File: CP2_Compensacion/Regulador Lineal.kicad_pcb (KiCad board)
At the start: 2 copper layers, 21 parts, among them Q1 BD140, Q10 BD139, Q2 BD140, Q3 BD139, Q4 BD139, Q5 TIP42C, Q6 BD139, Q7 BD139, Q8 BD139

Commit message: Add files via upload
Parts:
- removed RL1: 10, Resistor_THT:R_Axial_DIN0204_L3.6mm_D1.6mm_P5.08mm_Horizontal
- removed Vin1: 9.5, Connector_PinHeader_1.00mm:PinHeader_1x01_P1.00mm_Horizontal
- removed Vref1: 2.5, Connector_PinHeader_1.00mm:PinHeader_1x01_P1.00mm_Horizontal
- added J1: conn_vreg, Connector_PinHeader_1.00mm:PinHeader_1x01_P1.00mm_Vertical, F.Cu at (115.0, 88.0)
- added J2: conn_vreg, Connector_PinHeader_1.00mm:PinHeader_1x01_P1.00mm_Vertical, F.Cu at (115.0, 50.0)
- added J3: conn_rl_gnd, Connector_PinHeader_1.00mm:PinHeader_1x01_P1.00mm_Vertical, F.Cu at (173.0, 85.0)
- added J4: conn_rl, Connector_PinHeader_1.00mm:PinHeader_1x01_P1.00mm_Vertical, F.Cu at (171.0, 59.0)
- added R3: 470, Resistor_THT:R_Axial_DIN0204_L3.6mm_D1.6mm_P5.08mm_Horizontal, F.Cu at (115.0, 55.0)
- added U1: TL431LP, Package_TO_SOT_THT:TO-92_Inline, F.Cu at (115.0, 68.3)
- moved Q6 20.7 mm to (145.1, 55.3)
- moved C4 20.7 mm to (151.6, 66.0)
- moved Q1 20.7 mm to (124.8, 62.9)
- moved Q10 20.7 mm to (122.2, 88.3)
- moved Q2 20.7 mm to (140.0, 60.4)
- moved Q3 20.7 mm to (129.8, 68.0)
- moved Q7 20.7 mm to (137.6, 78.0)
- moved Q8 20.7 mm to (129.8, 88.3)
- moved R1 20.7 mm to (122.2, 73.1)
- moved R2 20.7 mm to (151.6, 77.5)
- moved R4 20.7 mm to (165.6, 54.4)
- moved R5 20.7 mm to (165.4, 80.7)
- moved R7 20.7 mm to (157.8, 53.4)
- moved R9 20.7 mm to (140.0, 50.2)
- moved Q4 20.7 mm to (134.9, 68.0)
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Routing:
- net Net-(Q5-B): track 50.8 -> 27.6 mm
- net Net-(J2-Pin_1): track 82.5 -> 61.8 mm
- net Net-(Q5-C): track 48.5 -> 28.5 mm
- net Net-(Q3-B): track 6.13 -> 20.4 mm
- net GND: track 14.5 -> 3.46 mm
- net Net-(J4-Pin_1): track 68.7 -> 65.3 mm
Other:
- board outline added: 64 x 51 mm

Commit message: Add files via upload
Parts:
- added J5: out, TerminalBlock_Phoenix:TerminalBlock_Phoenix_MKDS-1,5-2-5.08_1x02_P5.08mm_Horizontal, F.Cu at (166.3, 73.0)
- added J6: V1, Connector_PinHeader_2.54mm:PinHeader_1x01_P2.54mm_Vertical, F.Cu at (114.0, 68.0)
- added J7: in, TerminalBlock_Phoenix:TerminalBlock_Phoenix_MKDS-1,5-2-5.08_1x02_P5.08mm_Horizontal, F.Cu at (132.0, 50.2)
- C4: footprint Capacitor_SMD:CP_Elec_6.3x4.5 -> Capacitor_THT:C_Disc_D4.3mm_W1.9mm_P5.00mm
- J1: value conn_vreg -> I1; footprint Connector_PinHeader_1.00mm:PinHeader_1x01_P1.00mm_Vertical -> Connector_PinHeader_2.54mm:PinHeader_1x02_P2.54mm_Vertical
- J2: value conn_vreg -> I2; footprint Connector_PinHeader_1.00mm:PinHeader_1x01_P1.00mm_Vertical -> Connector_PinHeader_2.54mm:PinHeader_1x02_P2.54mm_Vertical
- J3: value conn_rl_gnd -> I3; footprint Connector_PinHeader_1.00mm:PinHeader_1x01_P1.00mm_Vertical -> Connector_PinHeader_2.54mm:PinHeader_1x02_P2.54mm_Vertical
- J4: value conn_rl -> gnd; footprint Connector_PinHeader_1.00mm:PinHeader_1x01_P1.00mm_Vertical -> Connector_PinHeader_2.54mm:PinHeader_1x01_P2.54mm_Vertical
- moved J1 60.8 mm to (169.0, 60.0), turned to 180 degrees
- moved J2 42.3 mm to (138.0, 85.5)
- moved J4 40.4 mm to (144.0, 89.0)
- moved J3 29.7 mm to (145.0, 75.0), turned to 180 degrees
- moved R3 13.1 mm to (119.0, 67.5)
- moved U1 13.0 mm to (116.0, 81.3)
- moved R8 9.32 mm to (119.0, 54.5)
- moved Q5 6.54 mm to (155.9, 48.0)
- moved R1 3.66 mm to (125.0, 75.5)
- moved Q3 3.62 mm to (129.8, 71.6)
- moved Q1 3.09 mm to (124.5, 66.0)
- moved Q10 3.04 mm to (125.0, 89.5)
- moved R9 2.76 mm to (140.0, 47.5)
- moved R4 2.60 mm to (164.0, 56.5)
- moved C4 2.54 mm to (151.6, 68.5)
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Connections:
- J1 pad 1: GND -> Net-(J1-Pin_1)
- J3 pad 1: GND -> Net-(J3-Pin_1)
- J4 pad 1: Net-(J4-Pin_1) -> GND
- Q3 pad 1: Net-(Q3-E) -> Net-(J2-Pin_1)
- Q4 pad 1: Net-(Q3-E) -> Net-(J2-Pin_1)
- Q4 pad 3: Net-(Q4-B) -> Net-(J3-Pin_2)
- Q5 pad 2: Net-(Q5-C) -> Net-(J1-Pin_2)
- Q5 pad 3: Net-(J2-Pin_1) -> Net-(J7-Pin_2)
- Q6 pad 1: Net-(Q5-C) -> Net-(J1-Pin_2)
- Q7 pad 1: Net-(J4-Pin_1) -> Net-(J5-Pin_2)
- Q8 pad 2: Net-(Q3-E) -> Net-(J2-Pin_2)
- R3 pad 1: Net-(J2-Pin_1) -> Net-(J7-Pin_2)
- R4 pad 1: Net-(Q5-C) -> Net-(J1-Pin_1)
- R4 pad 2: Net-(J4-Pin_1) -> Net-(J5-Pin_2)
- R5 pad 1: Net-(J4-Pin_1) -> Net-(J5-Pin_2)
- R5 pad 2: Net-(Q4-B) -> Net-(J3-Pin_1)
- R6 pad 1: Net-(Q4-B) -> Net-(J3-Pin_1)
- R7 pad 1: Net-(Q5-C) -> Net-(J1-Pin_1)
- R8 pad 1: Net-(J2-Pin_1) -> Net-(J7-Pin_2)
- R9 pad 1: Net-(J2-Pin_1) -> Net-(J7-Pin_2)
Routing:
- net Net-(J7-Pin_2): track 0.00 -> 65.6 mm
- net Net-(J4-Pin_1): track 65.3 -> 0.00 mm
- net Net-(J5-Pin_2): track 0.00 -> 62.8 mm
- net Net-(J2-Pin_1): track 61.8 -> 23.8 mm
- net Net-(Q4-B): track 29.7 -> 0.00 mm
- net Net-(J1-Pin_2): track 0.00 -> 28.7 mm
- net Net-(Q5-C): track 28.5 -> 0.00 mm
- net Net-(Q3-E): track 25.0 -> 0.00 mm
- net Net-(J3-Pin_1): track 0.00 -> 20.5 mm
- net Net-(J1-Pin_1): track 0.00 -> 13.9 mm
- net Net-(J6-Pin_1): track 20.4 -> 30.5 mm
- net Net-(J3-Pin_2): track 0.00 -> 8.22 mm
- net Net-(J2-Pin_2): track 0.00 -> 6.41 mm
- net Net-(Q5-B): track 27.6 -> 21.4 mm
- net Net-(Q1-C): track 7.62 -> 13.0 mm
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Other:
- outline, holes or cut-outs redrawn

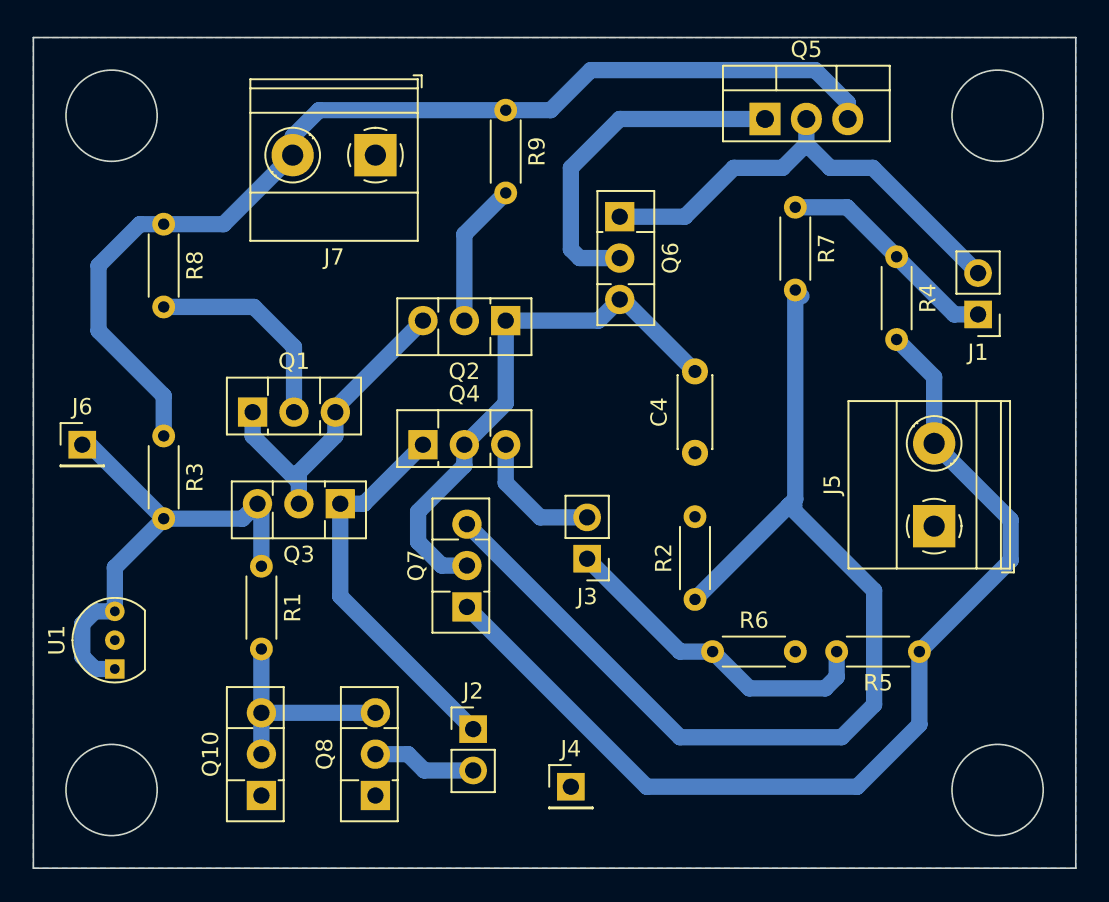
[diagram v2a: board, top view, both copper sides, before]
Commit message: Correcion del esquematico KiCad
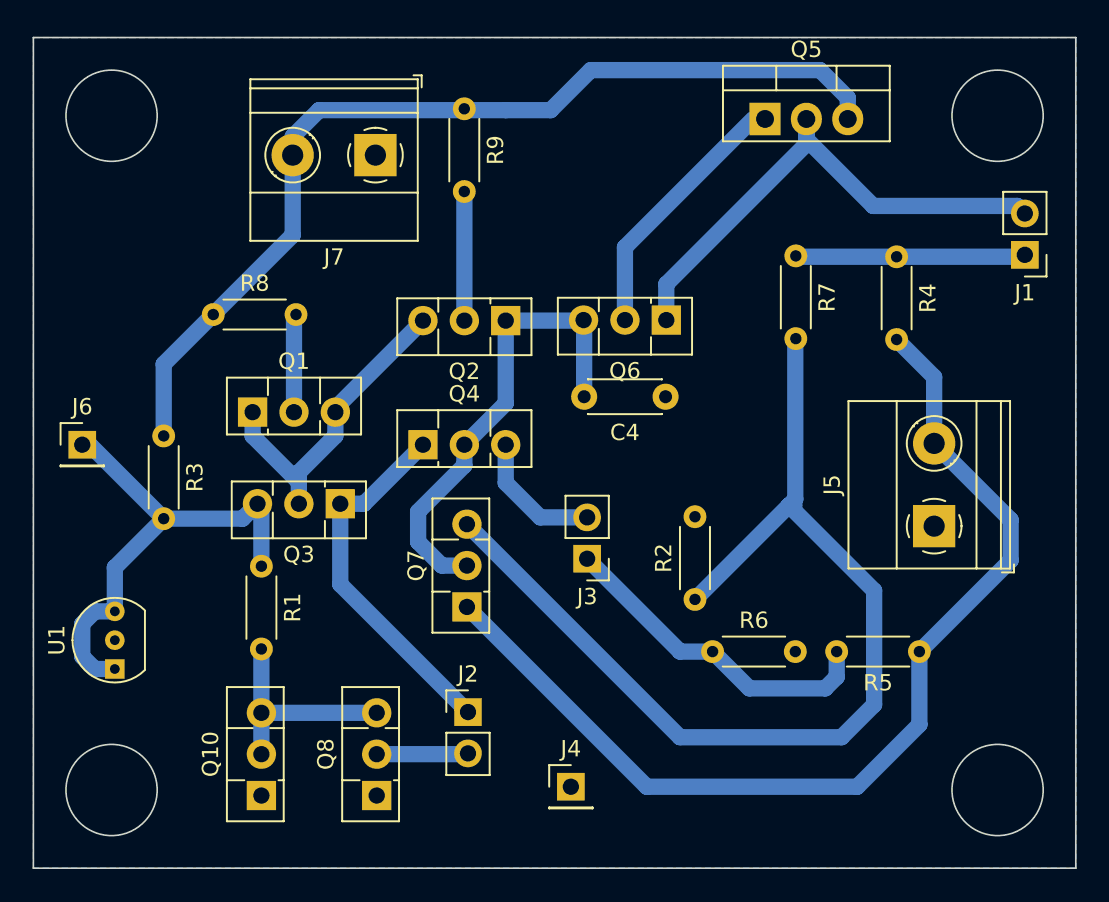
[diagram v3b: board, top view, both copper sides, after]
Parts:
- moved Q6 6.96 mm to (149.9, 60.3), turned to 180 degrees
- moved R8 6.33 mm to (122.0, 60.0), turned to 0 degrees
- moved J1 4.65 mm to (171.9, 56.3)
- moved C4 3.89 mm to (149.8, 65.1), turned to 180 degrees
- moved R7 2.99 mm to (157.8, 56.4)
- moved R9 2.55 mm to (137.5, 47.4)
- moved J2 1.09 mm to (137.7, 84.4)
- moved Q8 0.08 mm to (132.1, 89.5)
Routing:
- net Net-(Q1-C): track 13.0 -> 6.75 mm
- net Net-(J7-Pin_2): track 65.6 -> 59.4 mm
- net Net-(Q5-B): track 21.4 -> 16.3 mm
- net Net-(Q2-E): track 33.4 -> 28.9 mm
- net Net-(J1-Pin_2): track 28.7 -> 32.7 mm
- net Net-(Q7-B): track 68.1 -> 64.6 mm
- net Net-(J2-Pin_1): track 23.8 -> 22.7 mm
- net Net-(Q2-C): track 8.89 -> 7.93 mm
- net Net-(J2-Pin_2): track 6.41 -> 5.62 mm

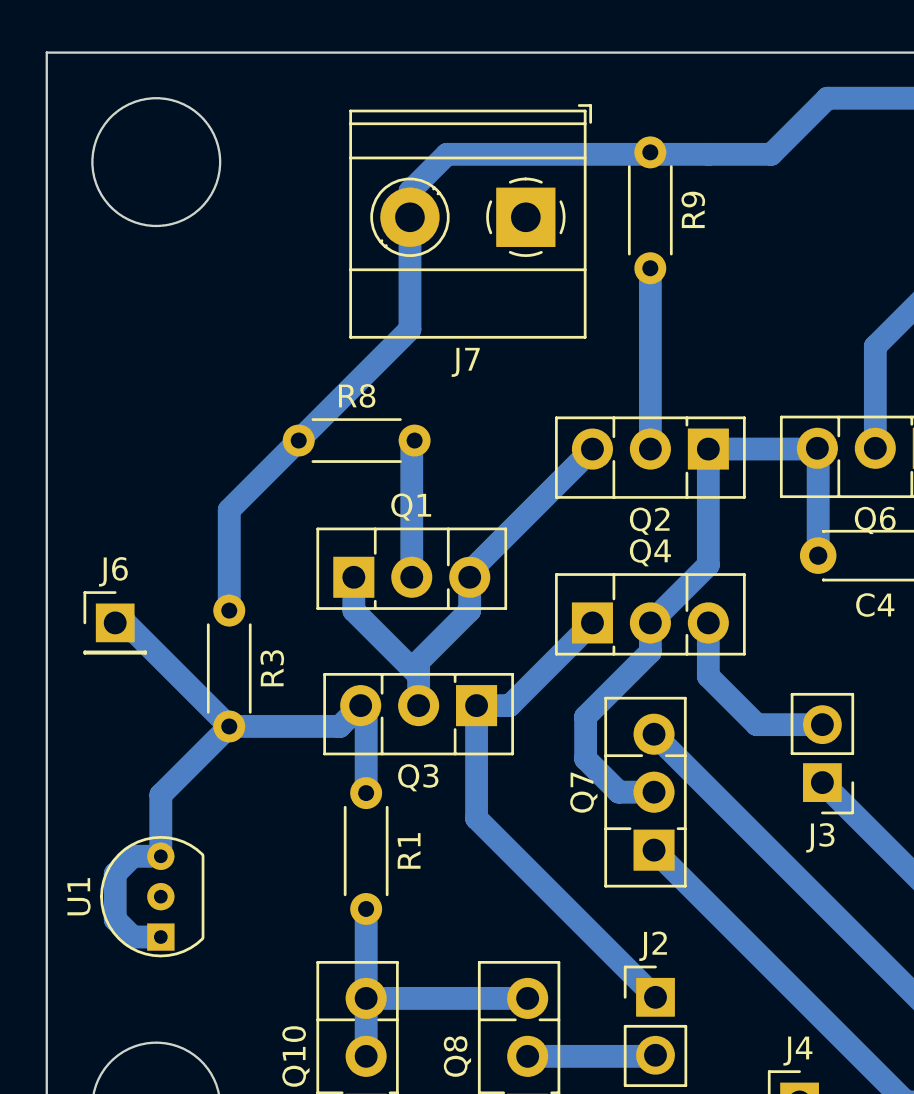
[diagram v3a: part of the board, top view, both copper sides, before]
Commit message: Correcion esquematico KiCad II
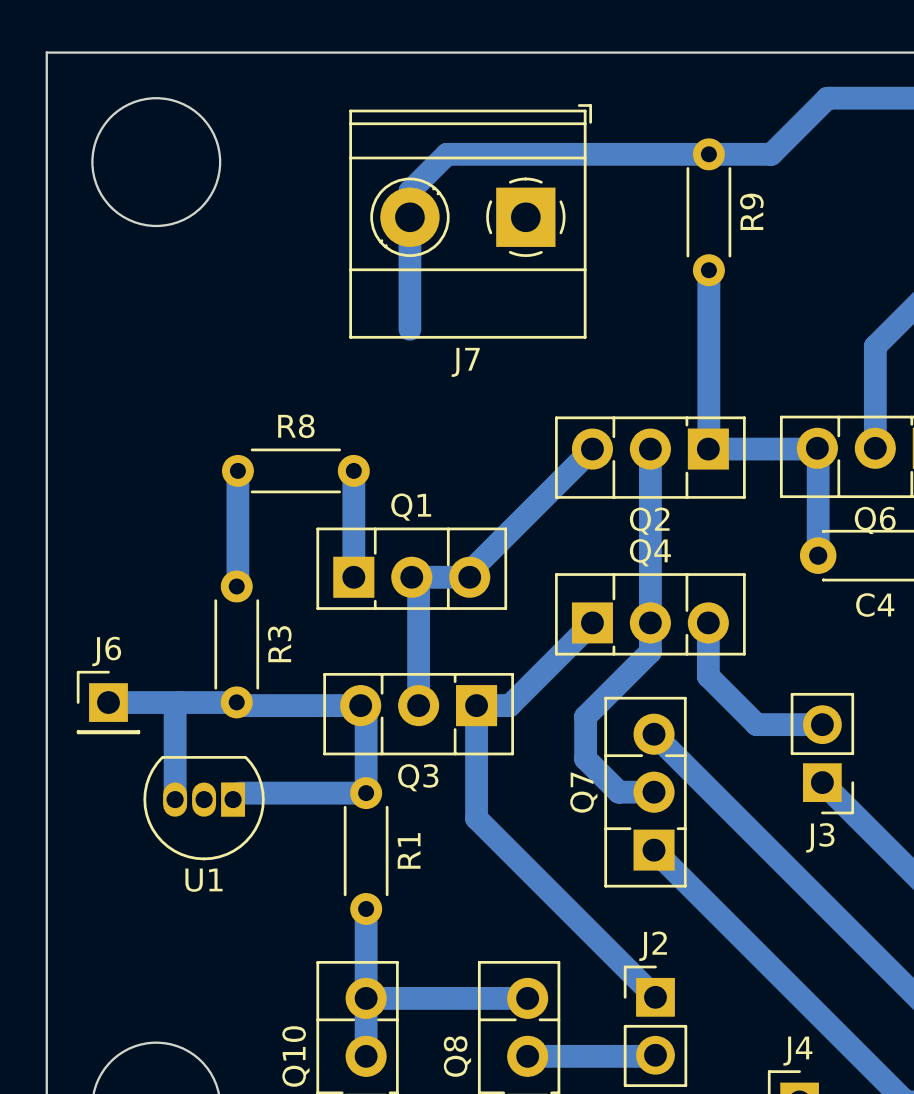
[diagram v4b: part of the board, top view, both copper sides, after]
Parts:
- moved U1 6.37 mm to (119.2, 75.7), turned to 180 degrees
- moved J6 3.50 mm to (113.7, 71.5)
- moved R8 2.98 mm to (119.4, 61.3)
- moved R9 2.57 mm to (140.0, 47.5)
- moved R3 1.11 mm to (119.3, 66.4)
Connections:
- C4 pad 2: Net-(Q2-E) -> Net-(Q2-C)
- Q1 pad 1: Net-(Q1-B) -> Net-(Q1-E)
- Q1 pad 2: Net-(Q1-C) -> Net-(Q1-B)
- Q4 pad 2: Net-(Q2-E) -> Net-(Q2-C)
- Q6 pad 3: Net-(Q2-E) -> Net-(Q2-C)
- Q7 pad 2: Net-(Q2-E) -> Net-(Q2-C)
- R8 pad 2: Net-(Q1-C) -> Net-(Q1-E)
- R9 pad 2: Net-(Q2-C) -> Net-(Q2-E)
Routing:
- net Net-(Q2-E): track 28.9 -> 17.4 mm
- net Net-(J7-Pin_2): track 59.4 -> 48.9 mm
- net Net-(Q2-C): track 7.93 -> 18.4 mm
- net Net-(Q1-C): track 6.75 -> 0.00 mm
- net Net-(J6-Pin_1): track 30.5 -> 25.7 mm
- net Net-(Q1-E): track 0.00 -> 4.66 mm
- net Net-(Q1-B): track 19.9 -> 16.8 mm

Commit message: Add files via upload
Corrección corte de tierra
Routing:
- net Net-(J7-Pin_2): track 48.9 -> 58.2 mm
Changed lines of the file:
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@@
 			(psa4output no)
 			(plot_black_and_white yes)
-			(plotinvisibletext no)
 			(sketchpadsonfab no)
 			(plotpadnumbers no)
@@
 	)
 	(segment
-		(start 126.92 50.22)
-		(end 126.92 55.131069)
+		(start 159.3 45)
+		(end 161 46.7)
 		(width 1)
 		(layer "B.Cu")
@@
 	)
 	(segment
-		(start 159.3 45)
-		(end 161 46.7)
+		(start 161 46.7)
+		(end 161 48)
 		(width 1)
 		(layer "B.Cu")
@@
 	)
 	(segment
-		(start 161 46.7)
-		(end 161 48)
+		(start 119.38 57.76)
+		(end 126.92 50.22)
+		(width 1)
+		(layer "B.Cu")
+		(net 4)
+	)
+	(segment
+		(start 119.38 61.336982)
+		(end 119.38 57.76)
 		(width 1)
 		(layer "B.Cu")
@@
 		(filled_areas_thickness no)
 		(fill yes
-			(thermal_gap 0.2)
+			(thermal_gap 0.5)
 			(thermal_bridge_width 0.5)
 		)
 		(polygon
 			(pts
-				(xy 111 43) (xy 175 43) (xy 175 94) (xy 111 94)
+				(xy 111 43) (xy 137 43) (xy 137 65) (xy 149.815442 65.052171) (xy 149.86 43) (xy 175 43) (xy 175 94)
+				(xy 111 94)
 			)
 		)

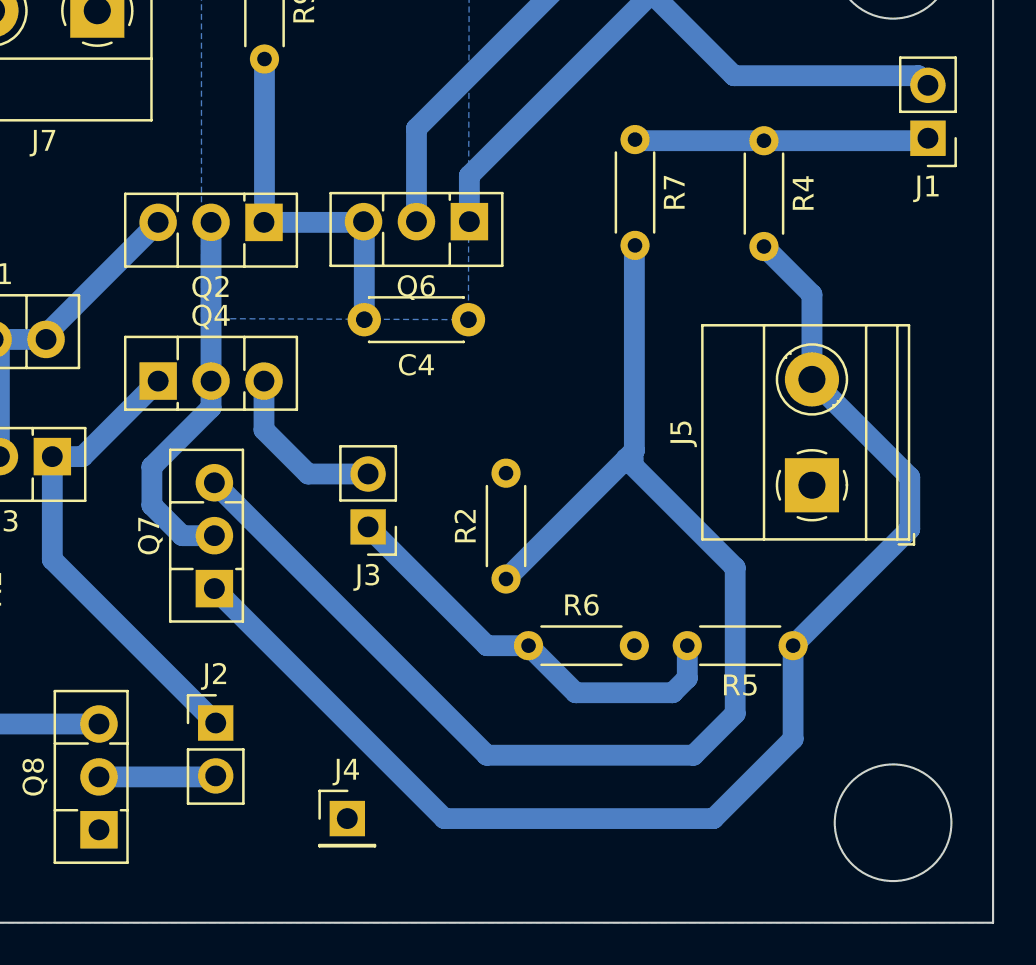
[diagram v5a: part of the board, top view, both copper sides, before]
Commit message: pista mal enrutada
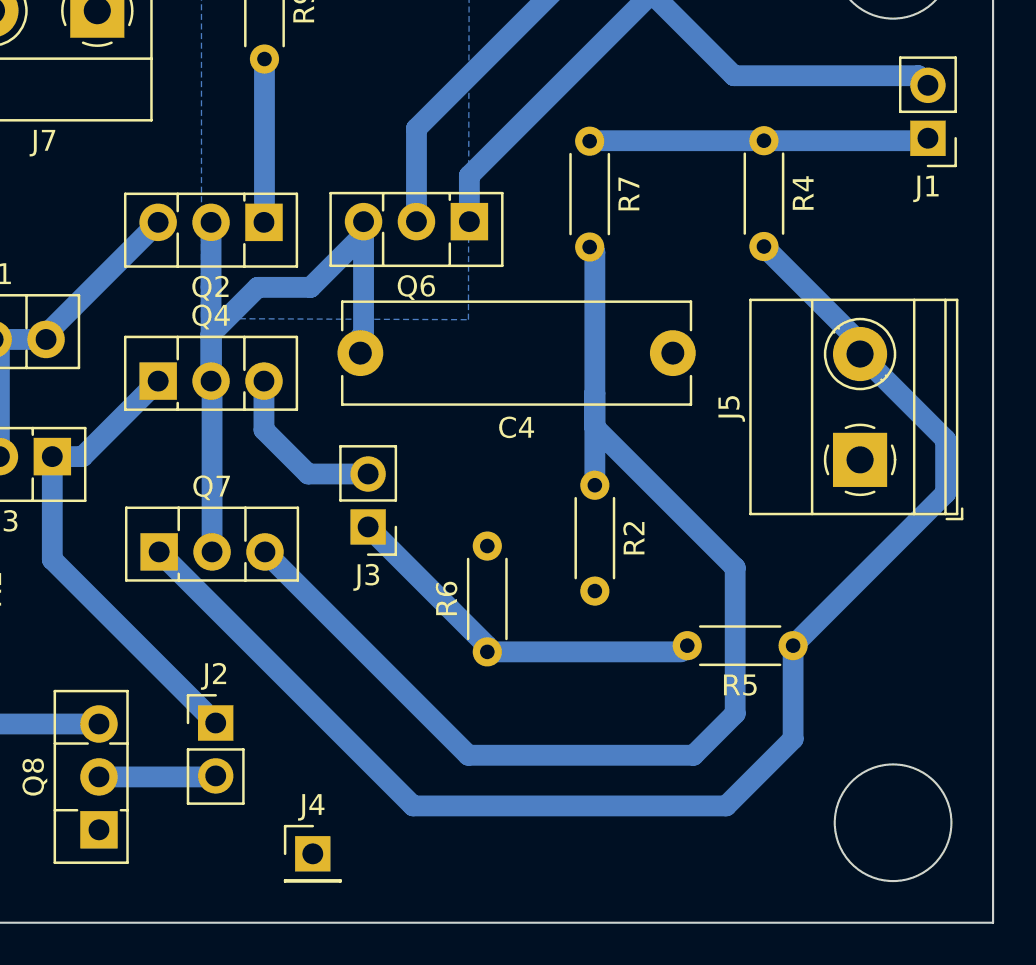
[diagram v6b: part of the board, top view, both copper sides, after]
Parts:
- C4: footprint Capacitor_THT:C_Disc_D4.3mm_W1.9mm_P5.00mm -> Capacitor_THT:C_Rect_L16.5mm_W4.7mm_P15.00mm_MKT
- moved C4 9.94 mm to (159.6, 66.7)
- moved R2 6.20 mm to (155.9, 73.0), turned to -90 degrees
- moved Q7 3.18 mm to (135.0, 76.2), turned to 0 degrees
- moved J5 2.61 mm to (168.6, 71.8)
- moved J4 2.37 mm to (142.3, 90.7)
- moved R7 2.18 mm to (155.6, 56.5)
- moved R6 2.00 mm to (150.7, 81.0), turned to 90 degrees
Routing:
- net Net-(Q2-C): track 18.4 -> 35.3 mm
- net Net-(Q2-E): track 17.4 -> 7.85 mm
- net Net-(Q7-B): track 64.6 -> 57.2 mm
- net Net-(J5-Pin_2): track 62.8 -> 67.1 mm
- net Net-(J3-Pin_1): track 20.5 -> 17.7 mm
- net Net-(J1-Pin_1): track 14.1 -> 16.3 mm
